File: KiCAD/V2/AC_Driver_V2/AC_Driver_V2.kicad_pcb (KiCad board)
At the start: 2 copper layers, 130.8 x 85 mm, 125 parts, among them J1-120VAC1 Screw_Terminal_01x02, J2 USART6, J2-HVDC2 Screw_Terminal_01x02, J3 USB_B_Micro, J4 Conn_01x05_Pin, J5 USART2, J6 Receiver, Q1 2N3904, SW1 SW_Push, SW2 SW_SPDT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

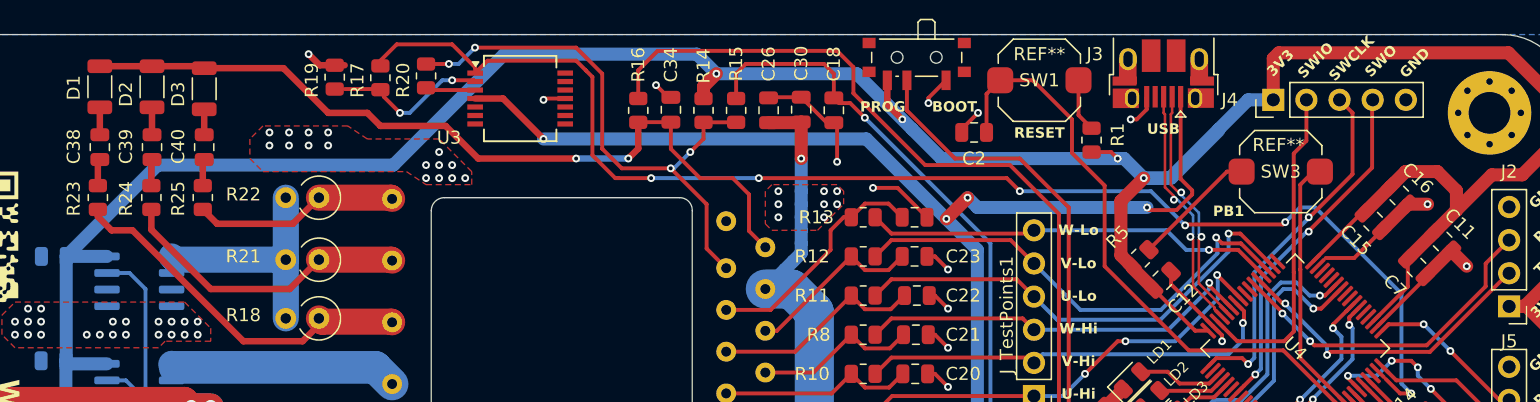
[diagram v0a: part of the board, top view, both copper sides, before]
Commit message: V2 tested and working - WIP
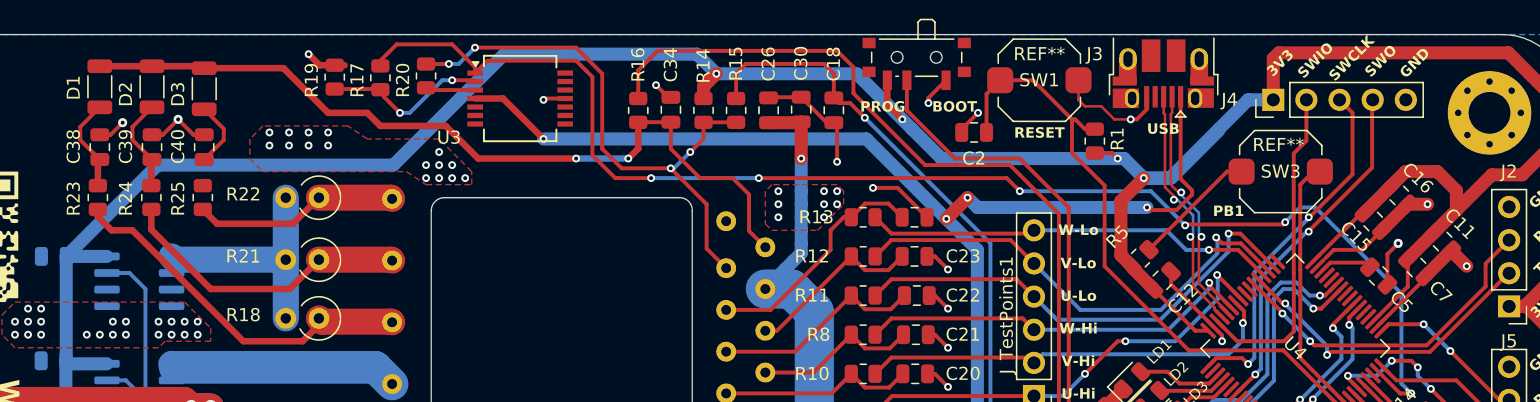
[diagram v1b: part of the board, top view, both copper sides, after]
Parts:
- added C5: 4u7, Capacitor_SMD:C_0805_2012Metric, F.Cu at (141.0, 48.5)
- moved R1 0.26 mm to (119.2, 38.2), turned to 90 degrees
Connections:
- C38 pad 1: Net-(D1-A) -> GND
- C38 pad 2: Net-(C38-Pad2) -> Net-(D1-A)
- C39 pad 1: Net-(D2-A) -> GND
- C39 pad 2: Net-(C39-Pad2) -> Net-(D2-A)
- C40 pad 1: Net-(D3-A) -> GND
- C40 pad 2: Net-(C40-Pad2) -> Net-(D3-A)
- R1 pad 1: Net-(R1-Pad1) -> +3.3V
- R1 pad 2: +3.3V -> /NRST
- R23 pad 2: Net-(C38-Pad2) -> Net-(D1-A)
- R24 pad 2: Net-(C39-Pad2) -> Net-(D2-A)
- R25 pad 2: Net-(C40-Pad2) -> Net-(D3-A)
- SW1 pad 1: Net-(R1-Pad1) -> GND
- U4 pad 30: unconnected-(U4-VCAP1-Pad30) -> Net-(U4-VCAP1)
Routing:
- net GND: track 144.3 -> 161.1 mm, vias 718 -> 721
- net Net-(D1-A): track 2.10 -> 7.30 mm
- net Net-(D2-A): track 2.10 -> 7.26 mm
- net Net-(R1-Pad1): track 4.09 -> 0.00 mm
- net Net-(U4-VCAP1): track 0.00 -> 4.06 mm
- net Net-(D3-A): track 1.95 -> 5.25 mm
- net Net-(C38-Pad2): track 2.06 -> 0.00 mm
- net /NRST: track 46.0 -> 48.1 mm
- net Net-(C40-Pad2): track 2.05 -> 0.00 mm
- net Net-(C39-Pad2): track 2.02 -> 0.00 mm

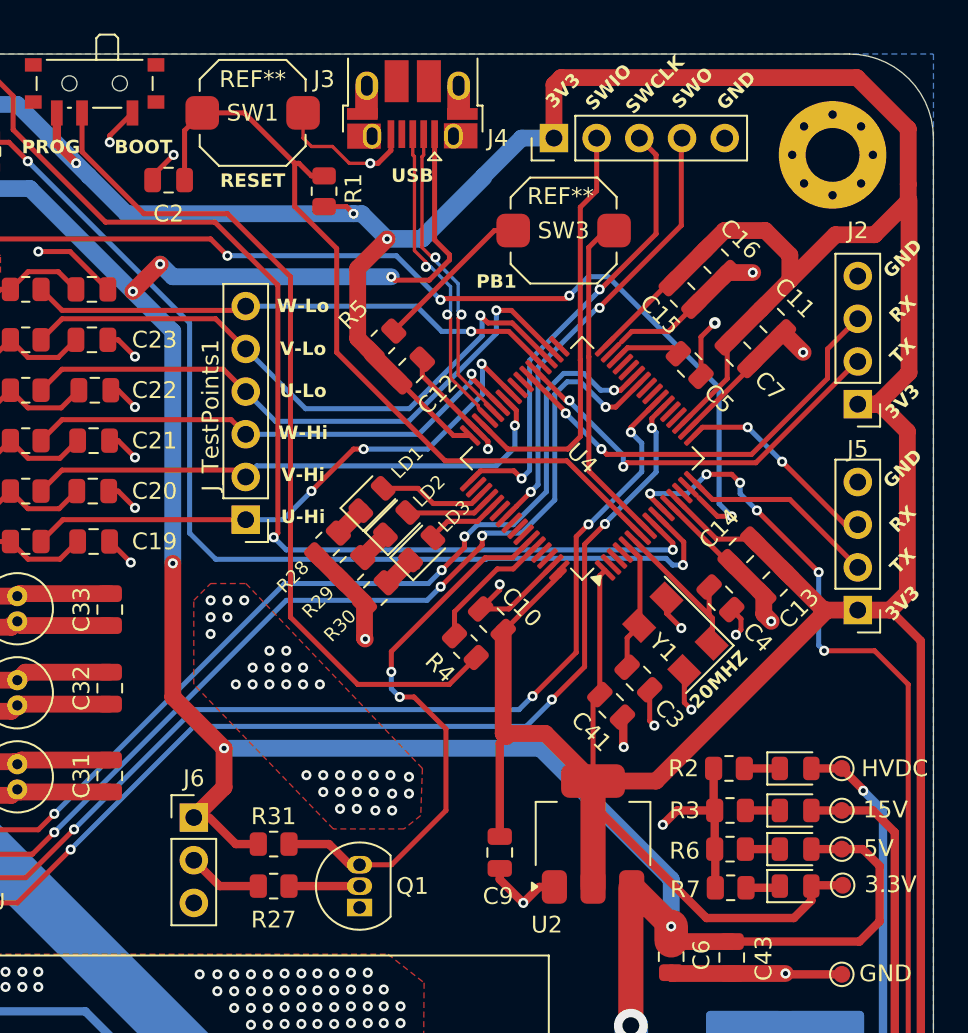
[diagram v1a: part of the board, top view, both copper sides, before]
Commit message: adds encoder
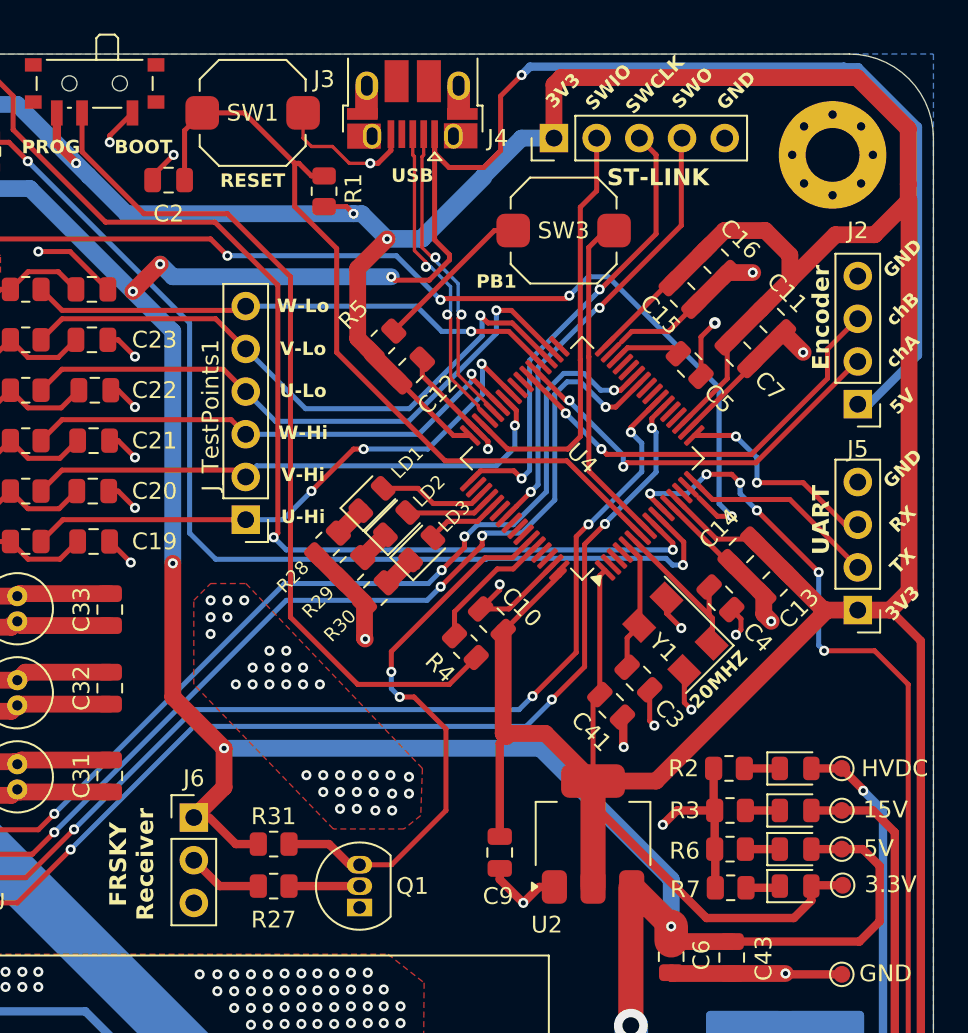
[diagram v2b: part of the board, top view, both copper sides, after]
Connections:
- J2 pad 1: +3.3V -> +5V
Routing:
- net +5V: track 175.1 -> 229.5 mm, vias 8 -> 9
- net +3.3V: track 414.3 -> 410.4 mm
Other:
- board text added: "5V"
- board text added: "Encoder"
- board text added: "FRSKY Receiver"
- board text added: "ST-LINK"
- board text added: "UART"
- board text added: "chA"
- board text added: "chB"
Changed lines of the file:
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@@
 			(layer "F.Fab")
 		)
-		(fp_text user "REF**"
-			(at 0 2 0)
-			(layer "F.SilkS")
-			(effects
-				(font
-					(size 1 1)
-					(thickness 0.15)
-				)
-			)
-		)
 		(fp_text user "${REFERENCE}"
 			(at 0.254 0 0)
@@
 			(layers "*.Cu" "*.Mask")
 			(remove_unused_layers no)
-			(net 16 "+3.3V")
+			(net 21 "+5V")
 			(pinfunction "Pin_1")
 			(pintype "passive")
@@
 		(tags "capacitor")
 		(property "Reference" "C11"
-			(at -0.008884 -1.908883 135)
+			(at -0.539214 -1.802817 135)
 			(layer "F.SilkS")
 			(effects
@@
 			(layer "F.Fab")
 		)
-		(fp_text user "REF**"
-			(at -0.181765 -2.040916 0)
-			(layer "F.SilkS")
-			(effects
-				(font
-					(size 1 1)
-					(thickness 0.15)
-				)
-			)
-		)
 		(fp_text user "${REFERENCE}"
 			(at 0.254 0 0)
@@
 		)
 	)
+	(gr_text "UART"
+		(at 149.4 59.8 90)
+		(layer "F.SilkS")
+		(effects
+			(font
+				(size 1 1)
+				(thickness 0.2)
+				(bold yes)
+			)
+			(justify left bottom)
+		)
+	)
 	(gr_text "SWO"
 		(at 141.5 32.35 45)
@@
 		)
 	)
-	(gr_text "TX"
+	(gr_text "chA"
 		(at 154 48 45)
 		(layer "F.SilkS")
@@
 		)
 	)
+	(gr_text "ST-LINK"
+		(at 136.075 37.925 0)
+		(layer "F.SilkS")
+		(effects
+			(font
+				(size 1 1)
+				(thickness 0.2)
+				(bold yes)
+			)
+			(justify left bottom)
+		)
+	)
 	(gr_text "3V3"
 		(at 133.8 32.5 45)
@@
 		)
 	)
-	(gr_text "3V3"
+	(gr_text "5V"
 		(at 154 51 45)
 		(layer "F.SilkS")
@@
 		)
 	)
-	(gr_text "RX"
+	(gr_text "chB"
 		(at 154 45.5 45)
 		(layer "F.SilkS")
@@
 		)
 	)
+	(gr_text "Encoder"
+		(at 149.4 48.8 90)
+		(layer "F.SilkS")
+		(effects
+			(font
+				(size 1 1)
+				(thickness 0.2)
+				(bold yes)
+			)
+			(justify left bottom)
+		)
+	)
 	(gr_text "V"
 		(at 35.1 61.65 270)
@@
 		)
 	)
+	(gr_text "FRSKY\nReceiver"
+		(at 109.2 78.2 90)
+		(layer "F.SilkS")
+		(effects
+			(font
+				(size 1 1)
+				(thickness 0.2)
+				(bold yes)
+			)
+			(justify bottom)
+		)
+	)
 	(gr_text "3V3"
 		(at 154 63 45)
@@
 	)
 	(segment
+		(start 154.05 61.95)
+		(end 154.05 38.7)
+		(width 1)
+		(layer "F.Cu")
+		(net 16)
+	)
+	(segment
 		(start 135.25 74.65)
 		(end 135.25 73.25)
@@
 	)
 	(segment
-		(start 152.92 63.08)
-		(end 153.95 62.05)
-		(width 1)
-		(layer "F.Cu")
-		(net 16)
-	)
-	(segment
 		(start 119.25 39.075)
 		(end 120.575 39.075)
@@
 	)
 	(segment
-		(start 153.95 62.05)
-		(end 153.95 52.45)
-		(width 1)
-		(layer "F.Cu")
-		(net 16)
-	)
-	(segment
 		(start 150.1 79.45)
 		(end 148.2875 79.45)
@@
 	)
 	(segment
-		(start 154.05 48.95)
-		(end 154.05 38.7)
-		(width 1)
-		(layer "F.Cu")
-		(net 16)
-	)
-	(segment
 		(start 139.698817 43.656498)
 		(end 135.96698 47.388335)
@@
 	)
 	(segment
-		(start 152.33 50.83)
-		(end 151 50.83)
-		(width 1)
-		(layer "F.Cu")
-		(net 16)
-	)
-	(segment
 		(start 146.959531 41.959531)
 		(end 145.5 40.5)
@@
 	)
 	(segment
-		(start 152.17 50.83)
-		(end 154.05 48.95)
-		(width 1)
-		(layer "F.Cu")
-		(net 16)
-	)
-	(segment
 		(start 149.17 63.08)
 		(end 148.973934 63.08)
@@
 	)
 	(segment
-		(start 151 50.83)
-		(end 152.17 50.83)
-		(width 1)
-		(layer "F.Cu")
-		(net 16)
-	)
-	(segment
 		(start 147.2 81.4)
 		(end 142 81.4)
@@
 	)
 	(segment
+		(start 152.92 63.08)
+		(end 154.05 61.95)
+		(width 1)
+		(layer "F.Cu")
+		(net 16)
+	)
+	(segment
 		(start 149.669062 40.75)
 		(end 146.959531 43.459531)
@@
 		(net 16)
 	)
-	(segment
-		(start 153.95 52.45)
-		(end 152.33 50.83)
-		(width 1)
-		(layer "F.Cu")
-		(net 16)
-	)
 	(via
 		(at 121 39.5)
@@
 	)
 	(segment
+		(start 126.685 36.75)
+		(end 125.825 35.89)
+		(width 0.3)
+		(layer "F.Cu")
+		(net 21)
+	)
+	(segment
 		(start 148.2375 77.3)
 		(end 151.3 77.3)
@@
 	)
 	(segment
+		(start 129.75 35.75)
+		(end 128.75 36.75)
+		(width 0.3)
+		(layer "F.Cu")
+		(net 21)
+	)
+	(segment
 		(start 143.5 82.8)
 		(end 139.95 82.8)
@@
 	)
 	(segment
+		(start 131 31.25)
+		(end 129.75 32.5)
+		(width 0.3)
+		(layer "F.Cu")
+		(net 21)
+	)
+	(segment
 		(start 110.25 68.25)
 		(end 113.3 71.3)
@@
 	)
 	(segment
+		(start 128.75 36.75)
+		(end 126.685 36.75)
+		(width 0.3)
+		(layer "F.Cu")
+		(net 21)
+	)
+	(segment
 		(start 139.95 82.8)
 		(end 139.9 82.75)
@@
 	)
 	(segment
+		(start 125.825 35.89)
+		(end 125.825 34.765)
+		(width 0.3)
+		(layer "F.Cu")
+		(net 21)
+	)
+	(segment
+		(start 129.75 32.5)
+		(end 129.75 35.75)
+		(width 0.3)
+		(layer "F.Cu")
+		(net 21)
+	)
+	(segment
 		(start 137.5 87.8)
 		(end 137.5 79.6)
@@
 	)
 	(via
+		(at 131 31.25)
+		(size 0.6)
+		(drill 0.3)
+		(layers "F.Cu" "B.Cu")
+		(net 21)
+	)
+	(via
 		(at 110.25 60.3)
 		(size 0.6)
@@
 	)
 	(segment
+		(start 150.215808 30.788266)
+		(end 151.038266 30.788266)
+		(width 0.5)
+		(layer "B.Cu")
+		(net 21)
+	)
+	(segment
 		(start 109.5 42.5)
 		(end 110.25 43.25)
@@
 	)
 	(segment
+		(start 154.578338 34.328338)
+		(end 154.578338 47.921662)
+		(width 0.5)
+		(layer "B.Cu")
+		(net 21)
+	)
+	(segment
 		(start 101.75 38)
 		(end 107.875 44.125)
@@
 	)
 	(segment
+		(start 131.5 30.75)
+		(end 150.177542 30.75)
+		(width 0.5)
+		(layer "B.Cu")
+		(net 21)
+	)
+	(segment
 		(start 137.525 89.785)
 		(end 137.525 87.825)
@@
 	)
 	(segment
+		(start 151.038266 30.788266)
+		(end 154.578338 34.328338)
+		(width 0.5)
+		(layer "B.Cu")
+		(net 21)
+	)
+	(segment
+		(start 150.177542 30.75)
+		(end 150.215808 30.788266)
+		(width 0.5)
+		(layer "B.Cu")
+		(net 21)
+	)
+	(segment
 		(start 110.25 43.25)
 		(end 123.25 43.25)
@@
 	)
 	(segment
+		(start 154.578338 47.921662)
+		(end 151.67 50.83)
+		(width 0.5)
+		(layer "B.Cu")
+		(net 21)
+	)
+	(segment
 		(start 110.25 46.5)
 		(end 107.875 44.125)
@@
 	)
 	(segment
+		(start 151.67 50.83)
+		(end 151 50.83)
+		(width 0.5)
+		(layer "B.Cu")
+		(net 21)
+	)
+	(segment
+		(start 131 31.25)
+		(end 131.5 30.75)
+		(width 0.5)
+		(layer "B.Cu")
+		(net 21)
+	)
+	(segment
 		(start 126.774999 45.699999)
 		(end 126.774999 49.274999)
@@
 	)
 	(segment
-		(start 144.45 52.2)
-		(end 141.761918 52.2)
+		(start 143.75 52.75)
+		(end 143.691637 52.691637)
 		(width 0.3)
 		(layer "F.Cu")
@@
 	)
 	(segment
-		(start 141.761918 52.2)
-		(end 141.270281 52.691637)
+		(start 150.25 58)
+		(end 151 58)
 		(width 0.3)
 		(layer "F.Cu")
@@
 	)
 	(segment
-		(start 150.25 58)
-		(end 151 58)
+		(start 147.75 55.5)
+		(end 150.25 58)
 		(width 0.3)
 		(layer "F.Cu")
@@
 	)
 	(segment
-		(start 146.5 54.25)
-		(end 150.25 58)
+		(start 143.691637 52.691637)
+		(end 141.270281 52.691637)
+		(width 0.3)
+		(layer "F.Cu")
+		(net 28)
+	)
+	(segment
+		(start 145 55.5)
+		(end 147.75 55.5)
 		(width 0.3)
 		(layer "F.Cu")
@@
 	)
 	(via
-		(at 146.5 54.25)
+		(at 145 55.5)
 		(size 0.6)
 		(drill 0.3)
@@
 	)
 	(via
-		(at 144.45 52.2)
+		(at 143.75 52.75)
 		(size 0.6)
 		(drill 0.3)
@@
 	)
 	(segment
-		(start 146.5 54.25)
-		(end 144.45 52.2)
+		(start 145 54)
+		(end 145 55.5)
+		(width 0.3)
+		(layer "B.Cu")
+		(net 28)
+	)
+	(segment
+		(start 143.75 52.75)
+		(end 145 54)
 		(width 0.3)
 		(layer "B.Cu")
